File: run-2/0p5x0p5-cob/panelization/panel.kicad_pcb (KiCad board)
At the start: 4 copper layers, 98 x 92 mm, 216 parts, among them J1 Conn_01x01, J10 Conn_01x01, J11 Conn_01x01, J12 Conn_01x01, J2 Conn_01x01, J3 Conn_01x01, J4 Conn_01x01, J5 Conn_01x01, J6 Conn_01x01, J7 Conn_01x01, J8 Conn_01x01, J9 Conn_01x01

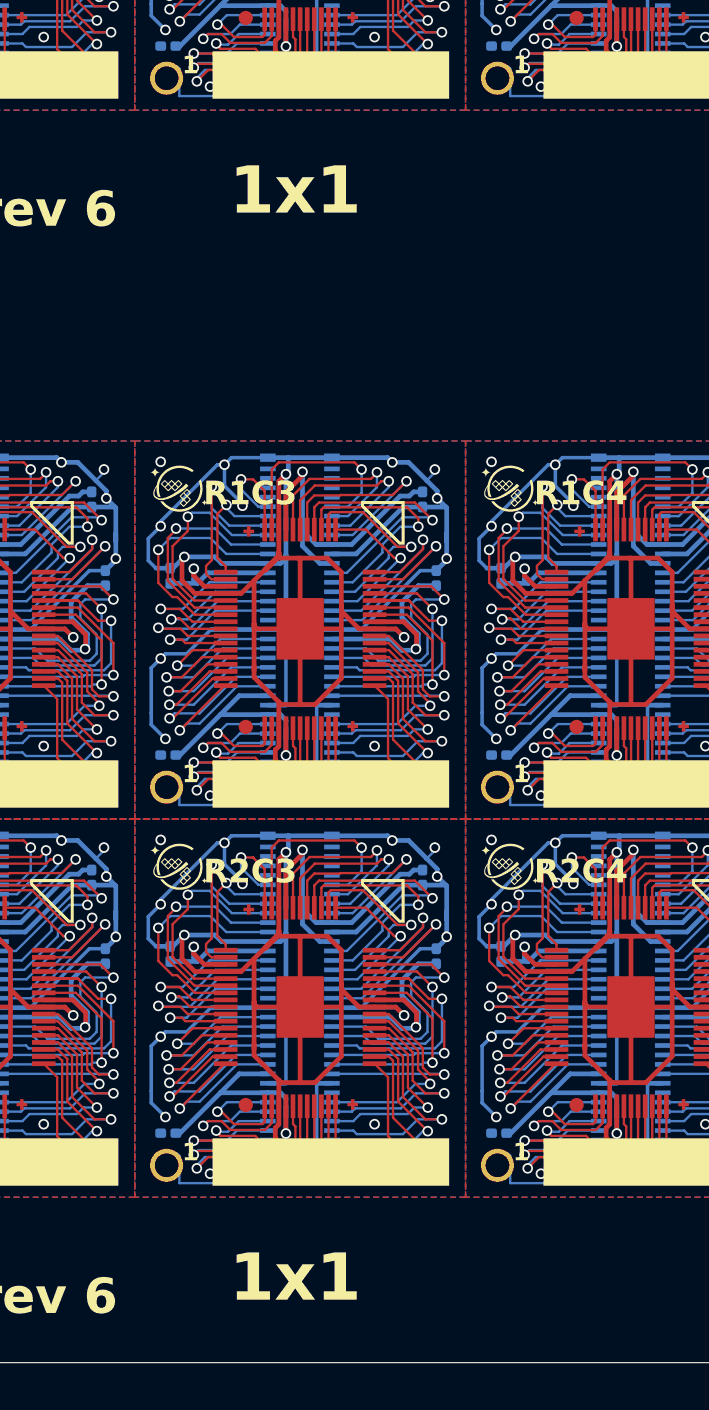
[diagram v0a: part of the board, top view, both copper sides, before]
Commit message: reexport panels and fix f.mask on p5xp5
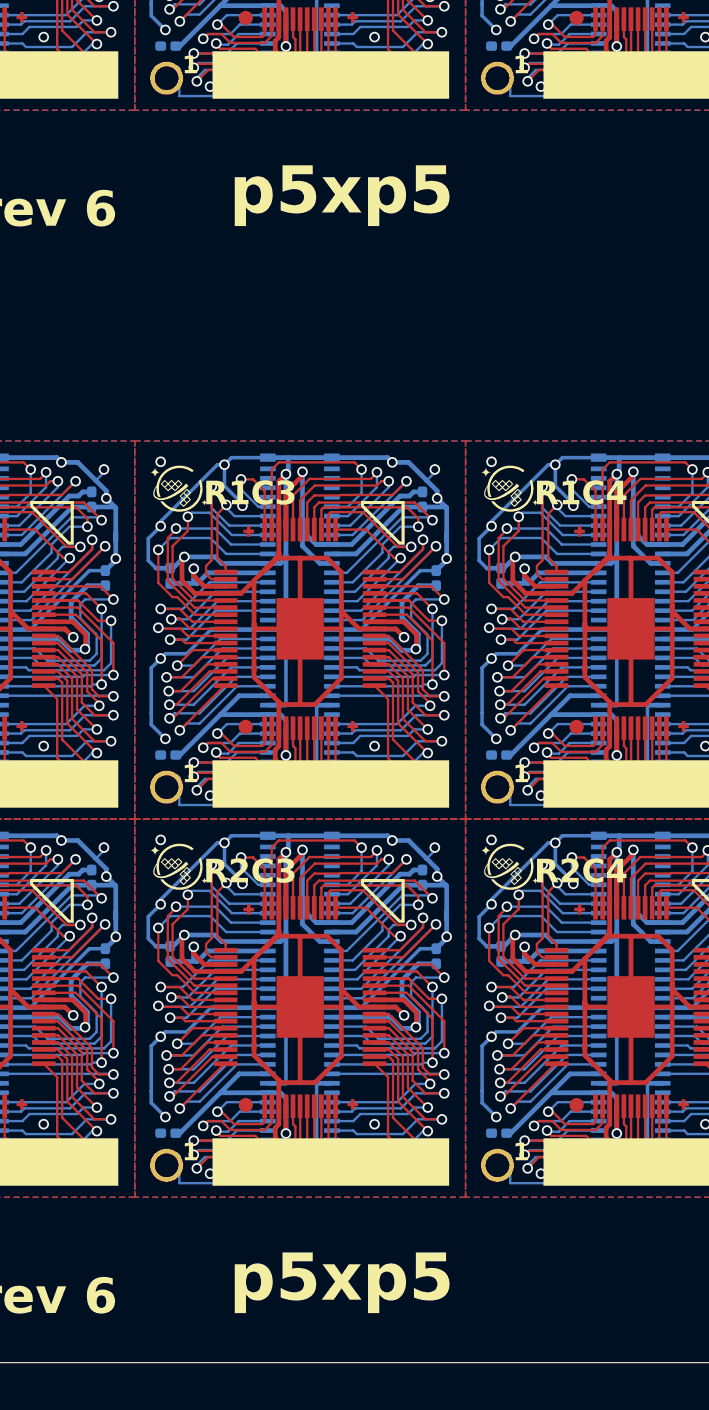
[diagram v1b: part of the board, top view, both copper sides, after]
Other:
- board text added: "p5xp5"
- board text removed: "1x1"
